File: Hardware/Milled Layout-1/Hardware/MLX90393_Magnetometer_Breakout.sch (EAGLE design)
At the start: 16 parts, among them U1 MLX90393_MAGNETOMETER

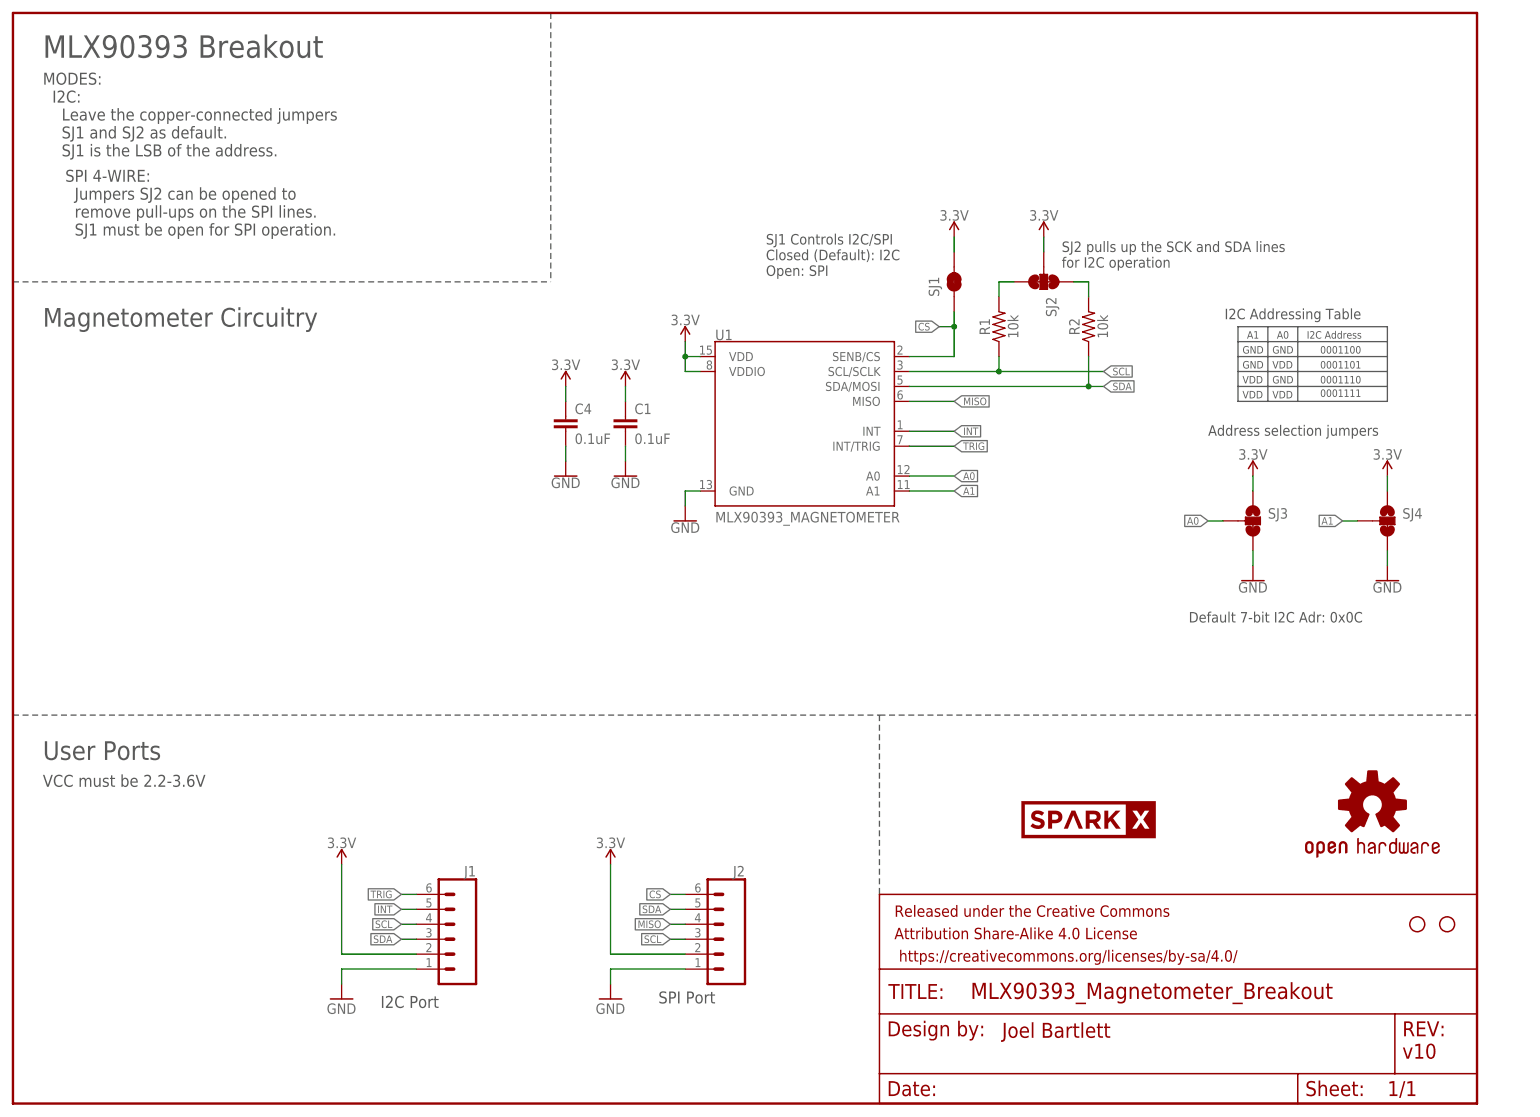
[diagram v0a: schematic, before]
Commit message: Adding new panel with updated silk and cream
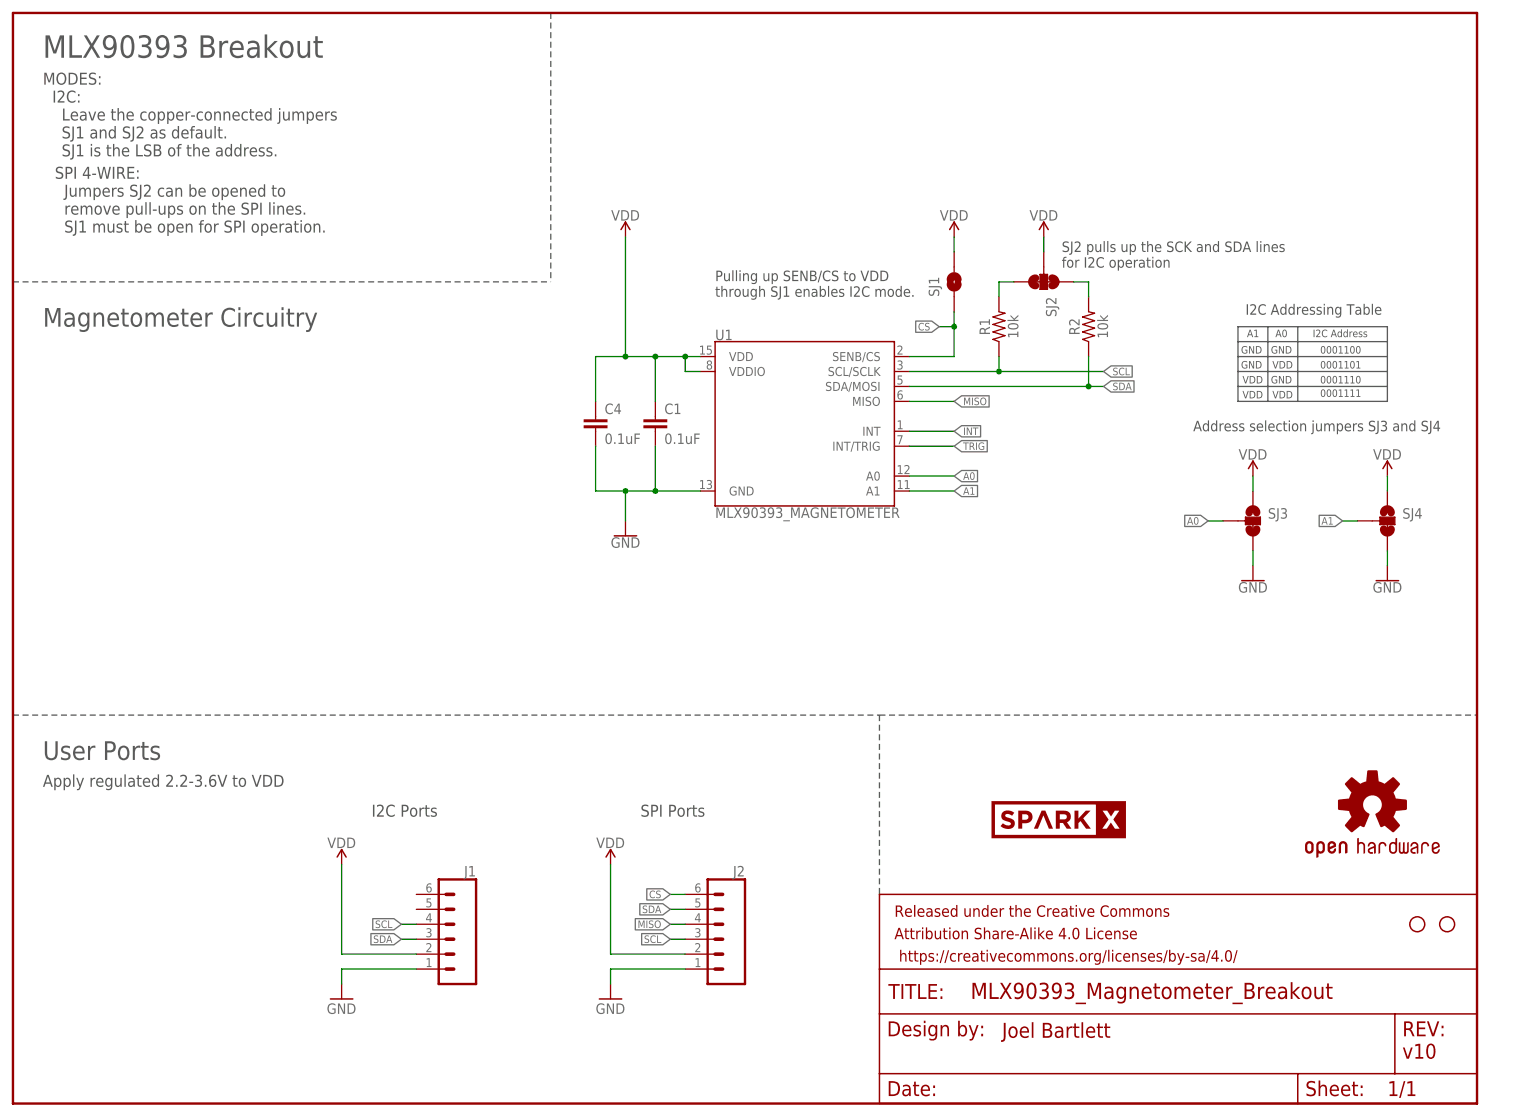
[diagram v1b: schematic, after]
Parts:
- SJ1: value JUMPER-SMT_2_NC_TRACE_SILK -> SOLDERJUMPERTRACE; device SparkFun-Jumpers:JUMPER-SMT_2_NC_TRACE_SILK -> SparkFun:SOLDERJUMPERTRACE
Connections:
- net 3.3V renamed VDD
- net INT: no longer J1.5
- net TRIG: no longer J1.6
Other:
- note added: "Address selection jumpers SJ3 and SJ4"
- note added: "Apply regulated 2.2-3.6V to VDD"
- note added: "I2C Ports"
- note added: "Pulling up SENB/CS to VDD through SJ1 enables I2C mode."
- note added: "SPI Ports"
- note removed: "Address selection jumpers"
- note removed: "Default 7-bit I2C Adr: 0x0C"
- note removed: "I2C Port"
- note removed: "SJ1 Controls I2C/SPI Closed (Default): I2C Open: SPI"
- note removed: "SPI Port"
- note removed: "VCC must be 2.2-3.6V"
- moved on the sheet: C1, C4
